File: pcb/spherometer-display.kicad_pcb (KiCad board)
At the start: 2 copper layers, 34 x 14 mm, 15 parts, among them J1 Battery, J2 Indicator, J3 Disp, J4 Programming, Q1 NPN, Q2 NPN, SW1 UI-Button, U1 ATTINY85V-10SU

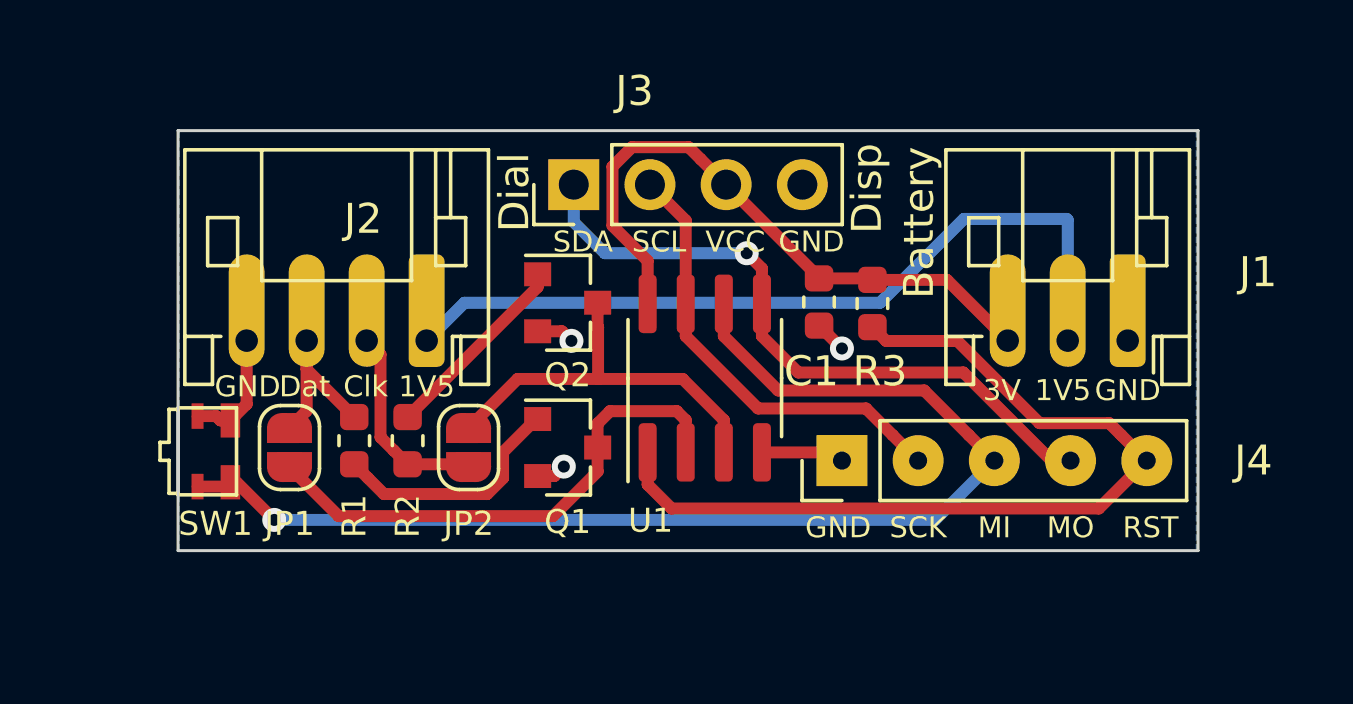
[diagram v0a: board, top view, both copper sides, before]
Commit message: Make bounding box around programming header more compact.
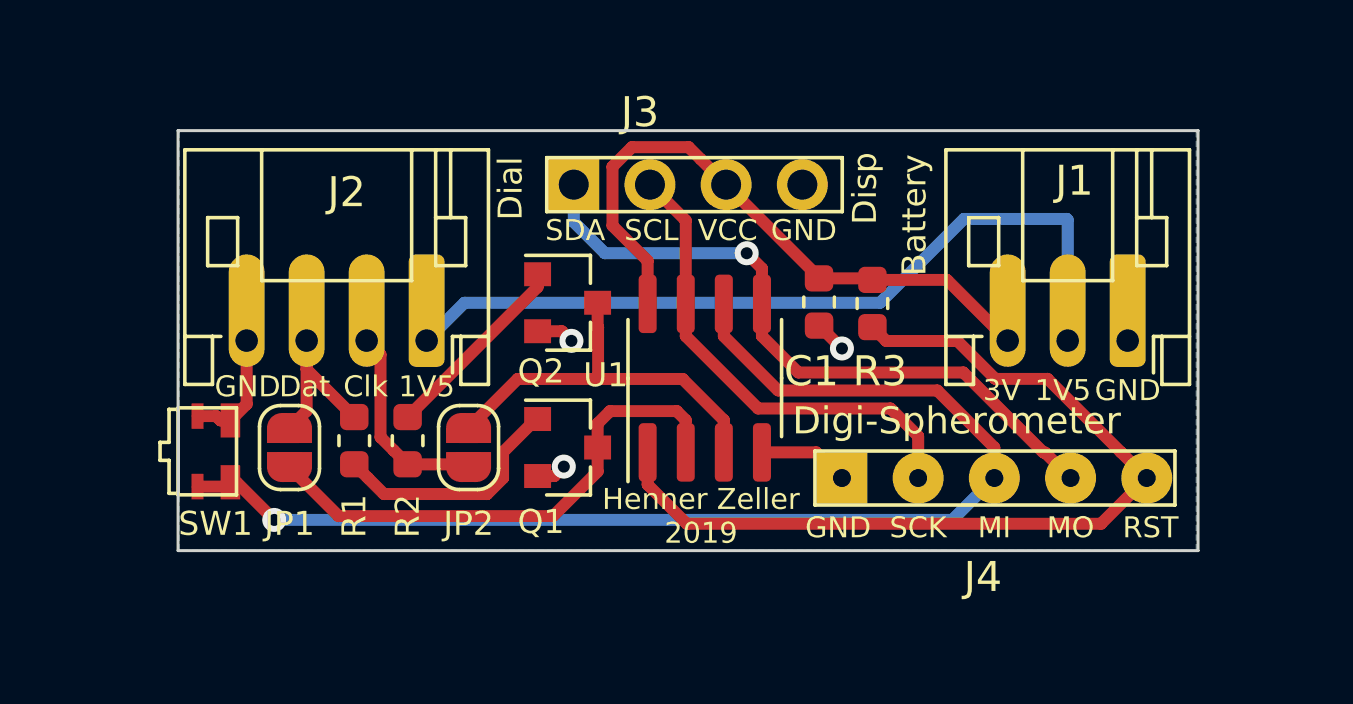
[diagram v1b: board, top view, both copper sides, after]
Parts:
- moved J4 0.58 mm to (87.6, 68.6)
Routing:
- net /SCL_SCK: track 15.0 -> 16.1 mm
- net /MISO: track 39.8 -> 40.4 mm
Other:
- board text added: "Digi-Spherometer"
- board text added: "Henner Zeller 2019"

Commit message: Swap pin sequence of indicator connector.
With a flat cable from the autolet indicator, the GND pin is towards
the center.
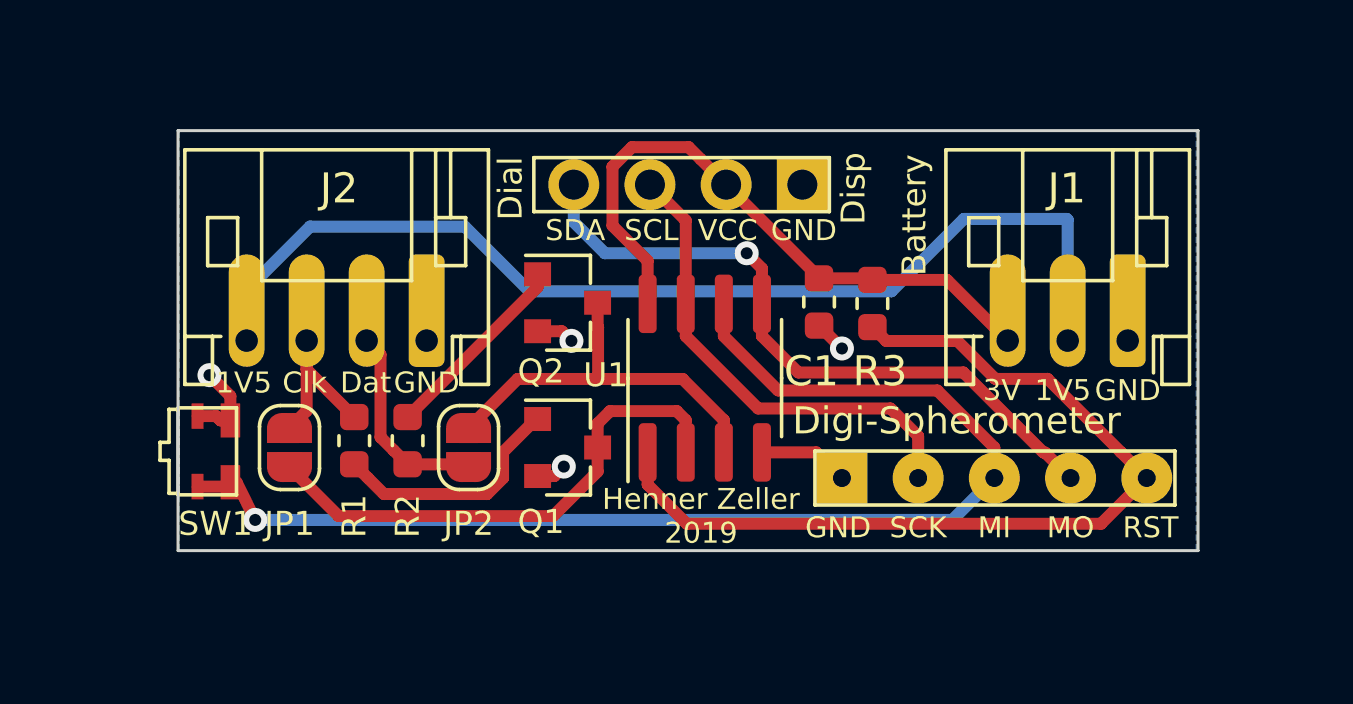
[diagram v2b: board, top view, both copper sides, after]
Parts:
- removed REF**: OSHW-Symbol_6.7x6mm_SilkScreen, Symbol:OSHW-Symbol_6.7x6mm_SilkScreen
- moved J3 7.62 mm to (86.3, 58.8), turned to 270 degrees
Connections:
- J2 pad 1: +1V5 -> GND
- J2 pad 2: /Clock -> /Data
- J2 pad 3: /Data -> /Clock
- J2 pad 4: GND -> +1V5
- J3 pad 1: /SDA_MOSI -> GND
- J3 pad 2: /SCL_SCK -> VCC
- J3 pad 3: VCC -> /SCL_SCK
- J3 pad 4: GND -> /SDA_MOSI
- JP1 pad 1: /Data -> /Clock
- JP2 pad 1: /Clock -> /Data
- R1 pad 2: /Data -> /Clock
- R2 pad 2: /Clock -> /Data
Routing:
- net +1V5: track 27.1 -> 35.9 mm
- net GND: track 10.5 -> 9.37 mm, vias 3 -> 4

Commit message: Re-add OSHW symbol (it got lost as it was not locked).
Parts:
- added REF**: OSHW-Symbol_6.7x6mm_SilkScreen, Symbol:OSHW-Symbol_6.7x6mm_SilkScreen, B.Cu at (82.5, 66.3)

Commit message: Fix: Attiny85 is the huge 5.3mm SOIC-8 footprint.
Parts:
- U1: footprint Package_SO:SOIC-8_3.9x4.9mm_P1.27mm -> Package_SO:SOIC-8_5.23x5.23mm_P1.27mm
- moved U1 0.16 mm to (83.1, 65.4)
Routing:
- net VCC: track 21.2 -> 19.8 mm
- net Net-(JP2-Pad2): track 13.4 -> 14.5 mm
- net Net-(JP1-Pad2): track 17.5 -> 18.6 mm
- net /MISO: track 40.6 -> 41.8 mm
- net /SDA_MOSI: track 22.7 -> 22.1 mm
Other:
- board text added: "Henner Zeller"
- board text removed: "Henner Zeller 2019"

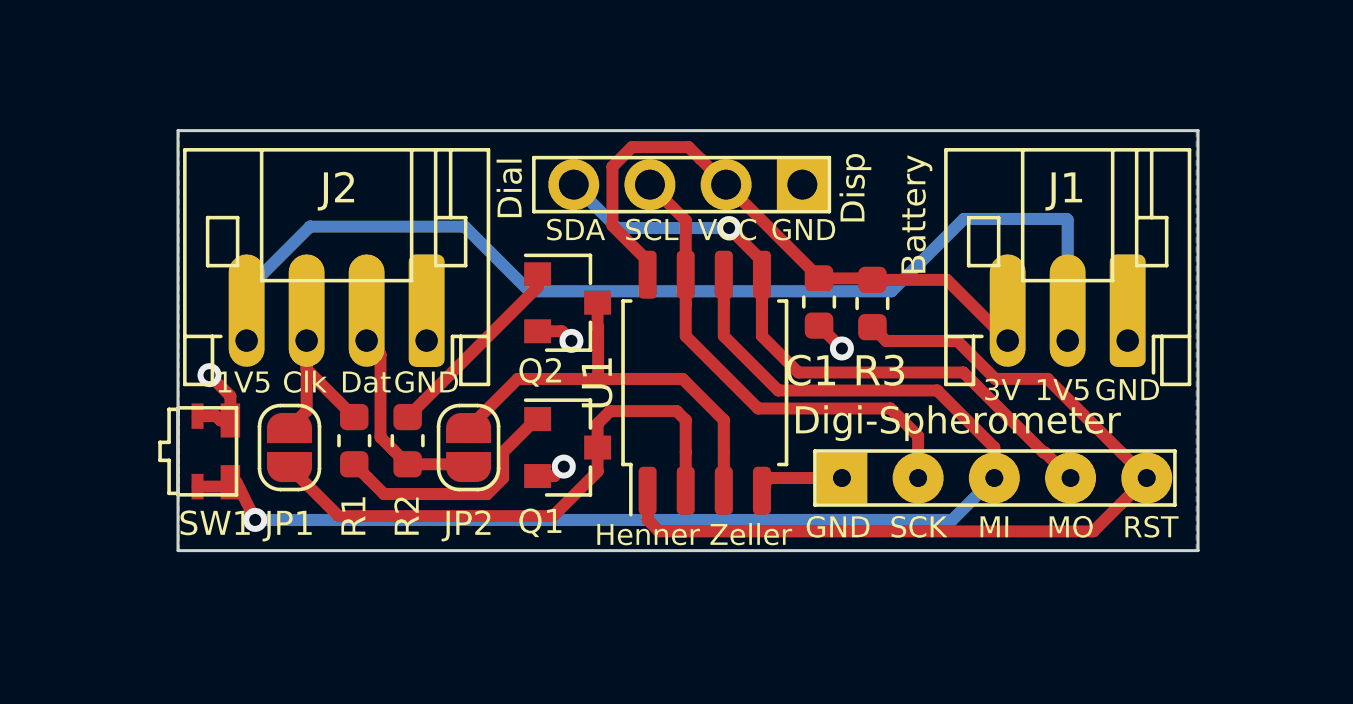
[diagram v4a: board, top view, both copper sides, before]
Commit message: New tactile button; slot-access cables; cutouts for components below.
o The old tactile button was too small and flimsy and disintegrated
  quickly. Use a new one.
o Cables are not connected anymore with JST connectors (too big), but
  instead slots are provided to solder them in. Also, some space
  above the board is provided for the cable access to minimize space-loss
  due to discomboulated cable entrance.
o Provide cutouts for places where on the 1.3" displays typically components
  are to be found.
o Make the board slightly less high as the row of passives in some displays
  starts a bit further up.

This is work-in-progress. Cleanup of silk-screen has to be done and
cut-outs need to be prettified. Also, GND is not connected everywhere yet.
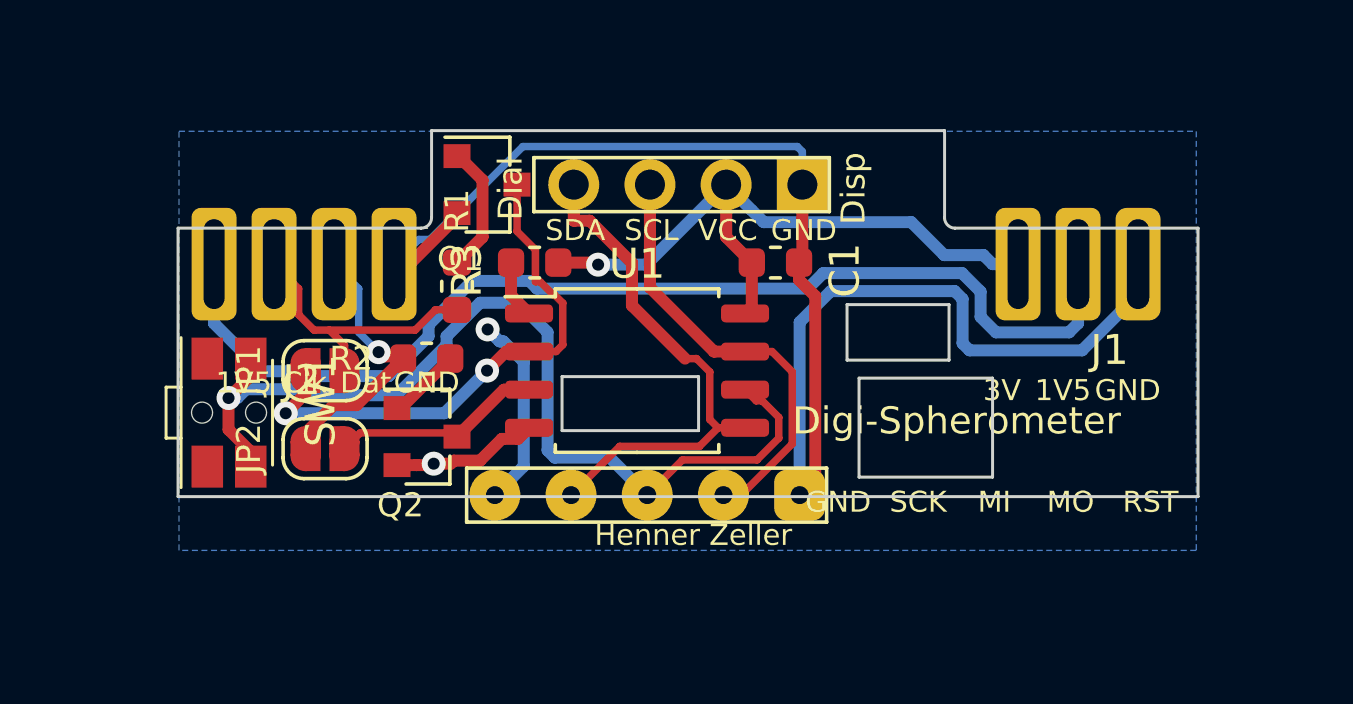
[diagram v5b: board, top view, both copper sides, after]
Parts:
- J1: footprint Connector_JST:JST_PH_S3B-PH-K_1x03_P2.00mm_Horizontal -> digi-spherometer:connect-edge-3slot-2mm
- J2: footprint Connector_JST:JST_PH_S4B-PH-K_1x04_P2.00mm_Horizontal -> digi-spherometer:connect-edge-4slot-2mm
- SW1: footprint digi-spherometer:EVPAV-Switch -> digi-spherometer:EVQP7-Switch
- moved R3 11.3 mm to (77.4, 61.4), turned to 180 degrees
- moved Q1 9.17 mm to (75.8, 58.8)
- moved J2 8.02 mm to (66.7, 60.2), turned to 0 degrees
- moved Q2 6.47 mm to (73.8, 67.2)
- moved R1 6.18 mm to (74.8, 62.2), turned to 270 degrees
- moved J1 5.24 mm to (93.5, 60.2), turned to 0 degrees
- moved JP2 4.78 mm to (70.4, 67.6), turned to 0 degrees
- moved JP1 2.82 mm to (70.4, 65.0), turned to 180 degrees
- moved R2 2.81 mm to (73.8, 64.6), turned to 180 degrees
- moved U1 2.29 mm to (80.8, 65.0), turned to 0 degrees
- moved SW1 2.13 mm to (67.2, 66.4)
- moved C1 1.96 mm to (85.4, 61.4), turned to 0 degrees
- moved J4 1.52 mm to (86.2, 69.2), turned to 270 degrees
- moved REF** 0.80 mm to (81.8, 66.3)
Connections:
- J1 pad 1: GND -> VCC
- J1 pad 3: VCC -> GND
- J2 pad 1: GND -> +1V5
- J2 pad 2: /Data -> /Clock
- J2 pad 3: /Clock -> /Data
- J2 pad 4: +1V5 -> GND
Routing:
- net GND: track 9.12 -> 55.0 mm, vias 4 -> 1
- net /Reset: track 29.9 -> 8.48 mm, vias 0 -> 1
- net /MISO: track 41.8 -> 31.6 mm
- net Net-(JP2-Pad2): track 14.5 -> 7.04 mm
- net /SDA_MOSI: track 22.1 -> 16.9 mm, vias 1 -> 0
- net Net-(Q2-Pad1): track 6.56 -> 2.46 mm
- net Net-(Q1-Pad1): track 8.07 -> 4.28 mm
- net /Clock: track 6.36 -> 9.36 mm
- net VCC: track 19.8 -> 22.5 mm, vias 0 -> 1
- net /Data: track 6.76 -> 9.25 mm, vias 0 -> 1
- net /SCL_SCK: track 16.1 -> 15.0 mm
- net +1V5: track 35.9 -> 36.8 mm
- net Net-(JP1-Pad2): track 18.6 -> 18.9 mm, vias 0 -> 2
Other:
- board size 34 x 14 mm -> 34 x 12.2 mm

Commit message: Some cleanup. Also add cut-outs to clear components on SH1106 display back.
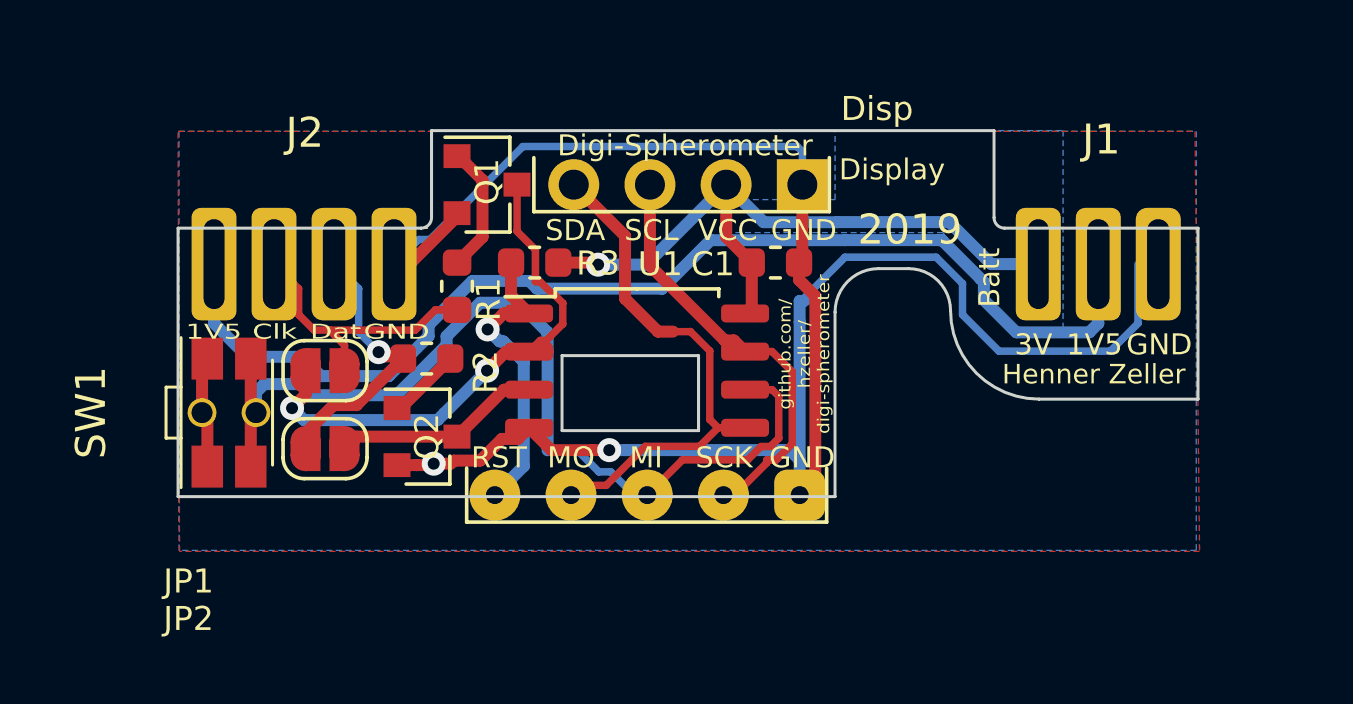
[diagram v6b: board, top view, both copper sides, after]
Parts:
- removed REF**: OSHW-Symbol_6.7x6mm_SilkScreen, Symbol:OSHW-Symbol_6.7x6mm_SilkScreen
- moved J1 0.67 mm to (94.2, 60.2)
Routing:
- net GND: track 55.0 -> 70.6 mm, vias 1 -> 2
- net +1V5: track 36.8 -> 40.7 mm
- net /Reset: track 8.48 -> 10.1 mm
- net /SCL_SCK: track 15.0 -> 13.5 mm
- net VCC: track 22.5 -> 23.1 mm
- net Net-(JP1-Pad2): track 18.9 -> 18.3 mm
- net /MISO: track 31.6 -> 31.4 mm, vias 1 -> 0
- added copper zone on F.Cu, net GND
- added copper zone on B.Cu, net VCC
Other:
- outline, holes or cut-outs redrawn
- board text added: "2019"
- board text added: "Batt"
- board text added: "Display"
- board text added: "github.com/ hzeller/ digi-spherometer"
- board text removed: "Dial"
- board text removed: "github.com/hzeller/digi-spherometer"
